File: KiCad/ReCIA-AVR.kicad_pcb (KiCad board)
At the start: 4 copper layers, 17.4 x 51.4 mm, 18 parts, among them U1 AVR128DA64-I_MR, U2 74AHCT1G17, U3 TLC2932AIPWR, U5 8520_DIP

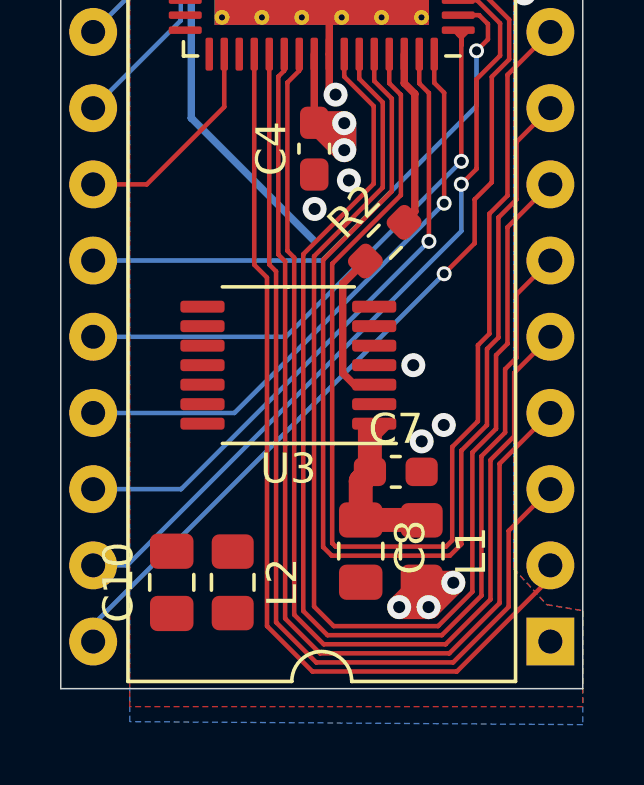
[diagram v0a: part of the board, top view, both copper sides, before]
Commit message: Add net and resistor between PDF_OUT and VCO_IN for the AVR-version
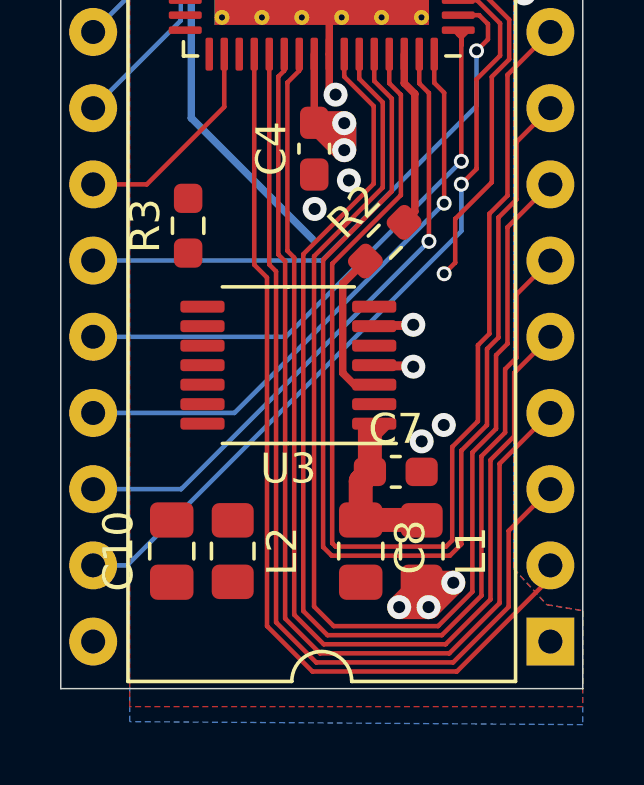
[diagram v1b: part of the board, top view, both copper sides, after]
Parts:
- added R3: 33, Resistor_SMD:R_0603_1608Metric_Pad0.98x0.95mm_HandSolder, F.Cu at (127.5, 93.3)
- moved C10 1.04 mm to (127.0, 104.1)
- moved L2 1.04 mm to (129.0, 104.1)
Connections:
- net /EXT-CLK renamed /VCO_OUT
- U3 pad 12: Net-(U3-Pad12) -> /VCO_IN
- U3 pad 6: Net-(U3-Pad6) -> /PFD_OUT
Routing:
- net CNT: track 28.6 -> 12.1 mm
- net /PFD_OUT: track 0.00 -> 10.5 mm, vias 0 -> 1
- net E-CLK: track 33.2 -> 35.9 mm

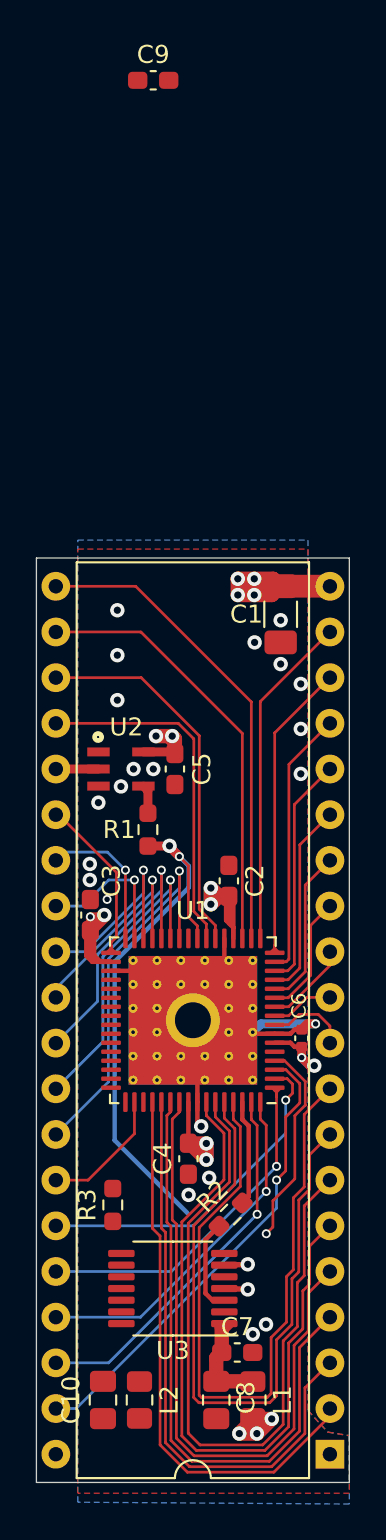
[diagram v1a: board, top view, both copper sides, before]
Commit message: Add resistor and net for PLL FIN-B clk-count input signal from AVR pin 5 (PA7)
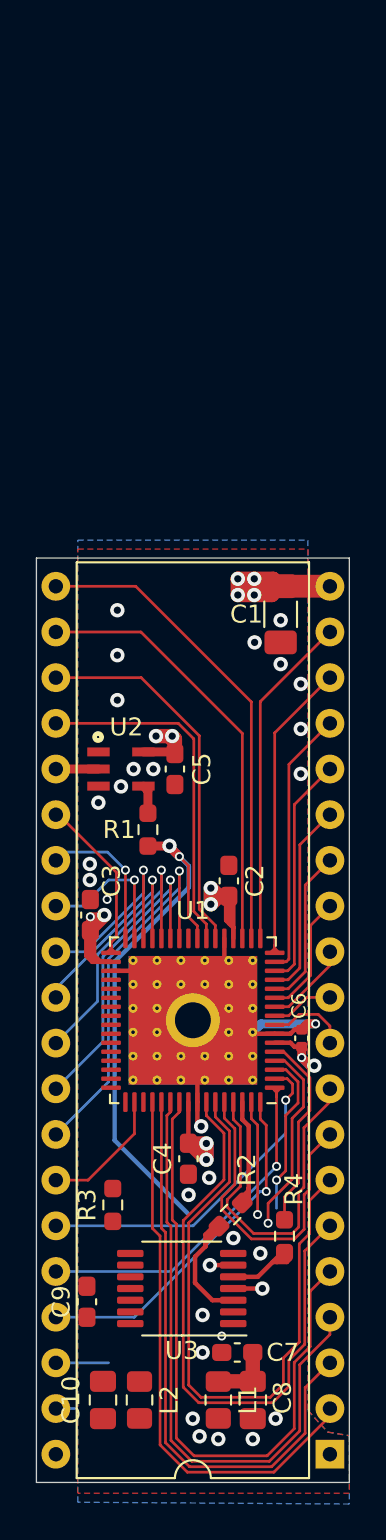
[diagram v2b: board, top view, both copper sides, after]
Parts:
- added R4: 33, Resistor_SMD:R_0603_1608Metric_Pad0.98x0.95mm_HandSolder, F.Cu at (137.1, 95.0)
- moved C9 68.0 mm to (126.1, 98.7), turned to 90 degrees
- moved C8 2.03 mm to (135.3, 104.1)
- moved L1 1.92 mm to (133.4, 104.1)
- moved U3 0.50 mm to (131.4, 97.9)
- turned C7 to 180 degrees
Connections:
- U1 pad 5: Net-(U1-Pad5) -> CLK_COUNT
- U3 pad 5: Net-(U3-Pad5) -> /FIN-B
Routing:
- net PA6: track 38.3 -> 17.9 mm
- net PA7: track 39.8 -> 19.4 mm
- net SP: track 26.1 -> 10.2 mm
- net A0: track 21.0 -> 9.33 mm
- net CLK_COUNT: track 0.00 -> 10.9 mm
- net /FIN-B: track 0.00 -> 5.62 mm
- net PA4: track 38.9 -> 33.7 mm
- net PA5: track 40.4 -> 35.3 mm
- net VCC: track 54.2 -> 49.8 mm
- net /LOGIC_VDD: track 7.55 -> 4.04 mm
- net /PFD_OUT: track 10.5 -> 7.10 mm
- net /VCO_OUT: track 5.26 -> 8.40 mm
- net EXTCLK: track 5.90 -> 7.69 mm
- net E-CLK: track 35.9 -> 34.9 mm
- net CNT: track 12.1 -> 11.4 mm
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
